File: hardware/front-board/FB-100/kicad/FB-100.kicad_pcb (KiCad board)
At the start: 2 copper layers, 80 x 35 mm, 48 parts, among them J1 USB4105-GF-A, J2 SSD1306_I2C_MODULE_DNP, SW1 EVPBB4A9B000 SERVICE, SW2 EVPBB4A9B000 RESET, U1 LTC3212EDDB#TRPBF

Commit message: feat(platform): authorize unified EVT development
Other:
- board text added: "FB-100 REV.1 EVT - NOT FOR PRODUCTION"
- board text removed: "FB-100 Rev.1 LAYOUT-ONLY"
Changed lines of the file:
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@@
 	(gr_rect (start 52 6) (end 58 12) (stroke (width 0.15) (type dash)) (fill none) (layer "Cmts.User"))
 	(gr_rect (start 64 6) (end 70 12) (stroke (width 0.15) (type dash)) (fill none) (layer "Cmts.User"))
-	(gr_text "FB-100 Rev.1  LAYOUT-ONLY" (at 40 33.5 0) (layer "F.SilkS") (effects (font (size 1.2 1.2) (thickness 0.18))))
+	(gr_text "FB-100 REV.1 EVT - NOT FOR PRODUCTION" (at 40 33.5 0) (layer "F.SilkS") (effects (font (size 1.0 1.0) (thickness 0.16))))
 	(gr_text "USB PANEL KEEPOUT" (at -6 12.5 0) (layer "Cmts.User") (effects (font (size 1 1) (thickness 0.15))))
 	(gr_text "FFC BEND KEEPOUT" (at 90 11.5 0) (layer "Cmts.User") (effects (font (size 1 1) (thickness 0.15))))

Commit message: feat(hardware): start PB and LB EVT layouts
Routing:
- net CH_LED_9_A: track 0.00 -> 5.51 mm
- net CH_LED_8_A: track 0.00 -> 5.51 mm
- net CH_LED_7_A: track 0.00 -> 5.51 mm
- net CH_LED_6_A: track 0.00 -> 5.51 mm
- net CH_LED_5_A: track 0.00 -> 5.51 mm
- net CH_LED_4_A: track 0.00 -> 5.51 mm
- net CH_LED_3_A: track 0.00 -> 5.51 mm
- net CH_LED_2_A: track 0.00 -> 5.51 mm
- net CH_LED_1_A: track 0.00 -> 5.51 mm
- net CH_LED_10_A: track 0.00 -> 5.51 mm
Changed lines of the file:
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@@
 		(pad "" np_thru_hole circle (at 0 0) (size 2.7 2.7) (drill 2.7) (layers "*.Cu" "*.Mask"))
 	)
+	(segment (start 20.80 31.50) (end 21.05 26.00) (width 0.25) (layer "F.Cu") (net 4))
+	(segment (start 25.80 31.50) (end 26.05 26.00) (width 0.25) (layer "F.Cu") (net 6))
+	(segment (start 30.80 31.50) (end 31.05 26.00) (width 0.25) (layer "F.Cu") (net 8))
+	(segment (start 35.80 31.50) (end 36.05 26.00) (width 0.25) (layer "F.Cu") (net 10))
+	(segment (start 40.80 31.50) (end 41.05 26.00) (width 0.25) (layer "F.Cu") (net 12))
+	(segment (start 45.80 31.50) (end 46.05 26.00) (width 0.25) (layer "F.Cu") (net 14))
+	(segment (start 50.80 31.50) (end 51.05 26.00) (width 0.25) (layer "F.Cu") (net 16))
+	(segment (start 55.80 31.50) (end 56.05 26.00) (width 0.25) (layer "F.Cu") (net 18))
+	(segment (start 60.80 31.50) (end 61.05 26.00) (width 0.25) (layer "F.Cu") (net 20))
+	(segment (start 65.80 31.50) (end 66.05 26.00) (width 0.25) (layer "F.Cu") (net 3))
 	(gr_rect (start 0 0) (end 80 35) (stroke (width 0.1) (type default)) (fill none) (layer "Edge.Cuts"))
 	(gr_rect (start -12 13.5) (end 0 21.5) (stroke (width 0.15) (type dash)) (fill none) (layer "Cmts.User"))
@@
 	(gr_rect (start 52 6) (end 58 12) (stroke (width 0.15) (type dash)) (fill none) (layer "Cmts.User"))
 	(gr_rect (start 64 6) (end 70 12) (stroke (width 0.15) (type dash)) (fill none) (layer "Cmts.User"))
-	(gr_text "FB-100 REV.1 EVT - NOT FOR PRODUCTION" (at 40 33.5 0) (layer "F.SilkS") (effects (font (size 1.0 1.0) (thickness 0.16))))
+	(gr_text "FB-100 REV.1 EVT - NOT FOR PRODUCTION" (at 40 2.0 0) (layer "F.SilkS") (effects (font (size 1.0 1.0) (thickness 0.16))))
 	(gr_text "USB PANEL KEEPOUT" (at -6 12.5 0) (layer "Cmts.User") (effects (font (size 1 1) (thickness 0.15))))
 	(gr_text "FFC BEND KEEPOUT" (at 90 11.5 0) (layer "Cmts.User") (effects (font (size 1 1) (thickness 0.15))))

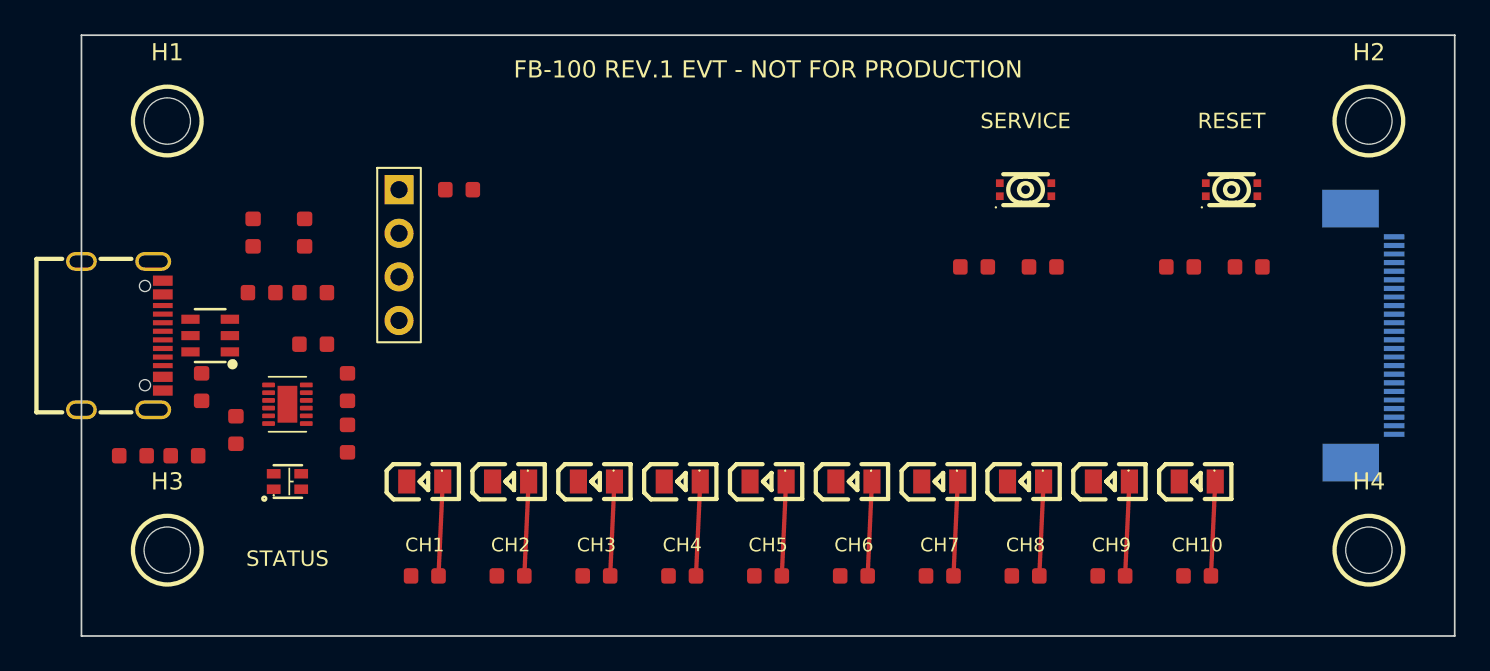
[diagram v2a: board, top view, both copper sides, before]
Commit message: feat(hardware): add EVT board routing milestones
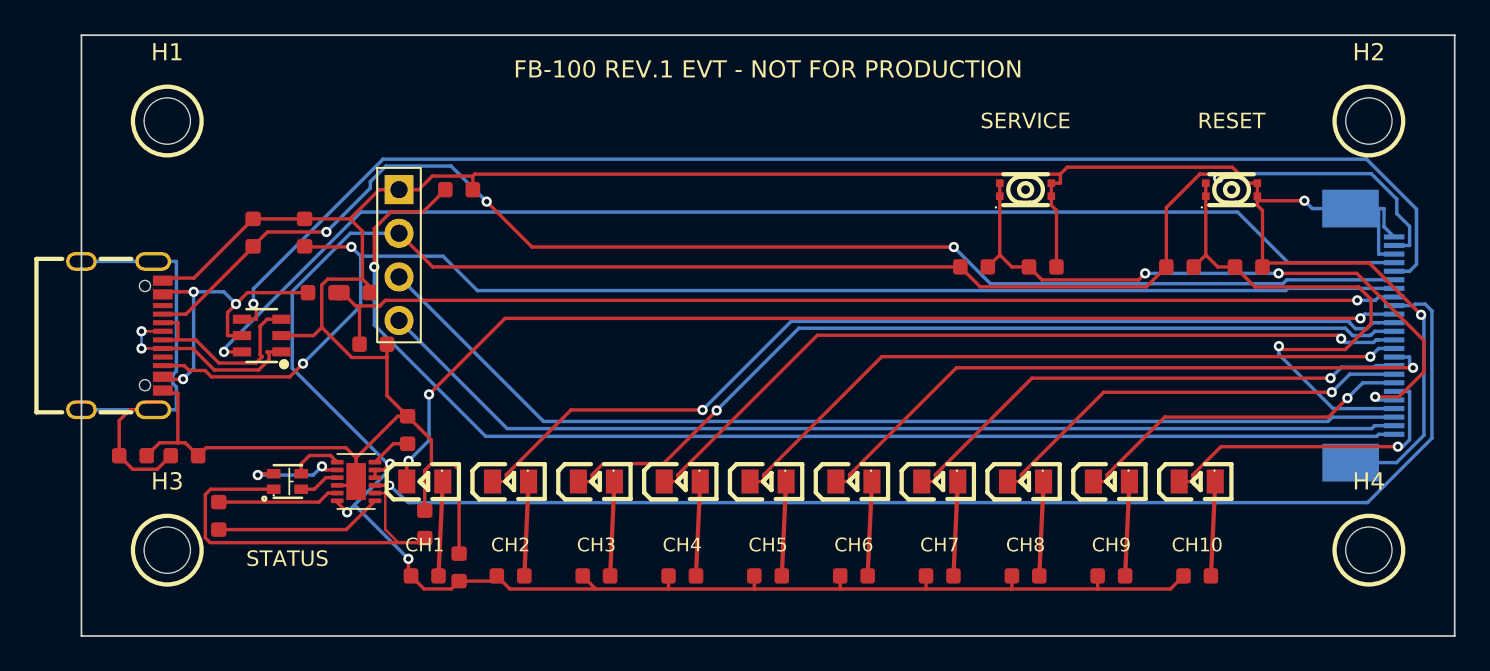
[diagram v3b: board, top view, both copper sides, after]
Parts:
- moved C3 12.3 mm to (22.0, 31.0)
- moved R16 10.0 mm to (19.0, 23.0)
- moved C4 7.57 mm to (8.00, 28.0)
- moved C5 6.73 mm to (20.0, 28.5)
- moved U1 6.02 mm to (16.0, 26.0), turned to 180 degrees
- moved C1 3.50 mm to (17.0, 18.0)
- moved R13 3.50 mm to (14.0, 15.0)
- moved D1 3.00 mm to (10.5, 17.5)
- moved R14 2.50 mm to (16.0, 15.0)
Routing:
- net GND: track 0.00 -> 172.9 mm, vias 0 -> 2
- net FB_3V3_OR_IO: track 0.00 -> 152.6 mm, vias 0 -> 4
- net USB_CC2: track 0.00 -> 81.0 mm, vias 0 -> 2
- net USB_D_N: track 0.00 -> 79.5 mm, vias 0 -> 1
- net USB_CC1: track 0.00 -> 78.5 mm, vias 0 -> 3
- net USB_D_P: track 0.00 -> 73.9 mm, vias 0 -> 1
- net STATUS_RGB_DATA: track 0.00 -> 73.3 mm, vias 0 -> 1
- net OLED_RST_OR_INT_DNP: track 0.00 -> 72.8 mm, vias 0 -> 1
- net USB_VBUS_DETECT_RAW: track 0.00 -> 64.4 mm, vias 0 -> 1
- net CH_LED_1: track 0.00 -> 63.8 mm, vias 0 -> 3
- net OLED_SCL: track 0.00 -> 61.6 mm
- net OLED_SDA: track 0.00 -> 60.6 mm
- net CH_LED_2: track 0.00 -> 57.0 mm, vias 0 -> 1
- net CH_LED_3: track 0.00 -> 51.7 mm, vias 0 -> 1
- net CH_LED_4: track 0.00 -> 46.5 mm, vias 0 -> 1
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
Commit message: hardware: finish FB-100 EVT layout checkpoint
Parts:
- moved C1 2.06 mm to (15.0, 18.5), turned to 90 degrees
- moved C3 2.00 mm to (22.0, 29.0)
- moved C4 1.50 mm to (9.50, 28.0)
- turned R13 to 90 degrees
- turned R14 to 90 degrees
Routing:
- net USB_D_P: track 73.9 -> 96.9 mm, vias 1 -> 4
- net USB_D_N: track 79.5 -> 97.0 mm, vias 1 -> 4
- net GND: track 172.9 -> 156.3 mm
- net USB_VBUS_DETECT_RAW: track 64.4 -> 70.6 mm
- net FB_3V3_OR_IO: track 152.6 -> 155.2 mm
- net RGB_CP: track 9.79 -> 8.29 mm
- net RGB_CM: track 7.12 -> 5.62 mm
- net USB_VBUS: track 19.0 -> 20.2 mm
- added copper zone on B.Cu, net GND
- added copper zone on F.Cu, net GND
- added copper zone on In1.Cu, net GND
- added copper zone on In2.Cu, net GND
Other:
- copper layers 2 -> 4

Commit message: feat: harden LB RF layout and CAN logging
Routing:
- net GND: vias 2 -> 5
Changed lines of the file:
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@@
 	(via (at 9.004800 15.662200) (size 0.600000) (drill 0.300000) (layers "F.Cu" "B.Cu") (net 43))
 	(via (at 74.324000 15.446500) (size 0.600000) (drill 0.300000) (layers "F.Cu" "B.Cu") (net 44))
+	(via (at 2.200000 17.750000) (size 0.600000) (drill 0.300000) (layers "F.Cu" "B.Cu") (net 22))
+	(via (at 11.800000 3.500000) (size 0.600000) (drill 0.300000) (layers "F.Cu" "B.Cu") (net 22))
+	(via (at 66.500000 5.500000) (size 0.600000) (drill 0.300000) (layers "F.Cu" "B.Cu") (net 22))
 	(zone
 		(net 22)
